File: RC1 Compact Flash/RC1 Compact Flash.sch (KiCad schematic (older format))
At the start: 16 parts, among them J1 Expansion, J2 ADDRESS, J3 ADAPTER, J4 POWER, J5 POWER, U1 74LS00, U3 74LS138, U4 74LS138

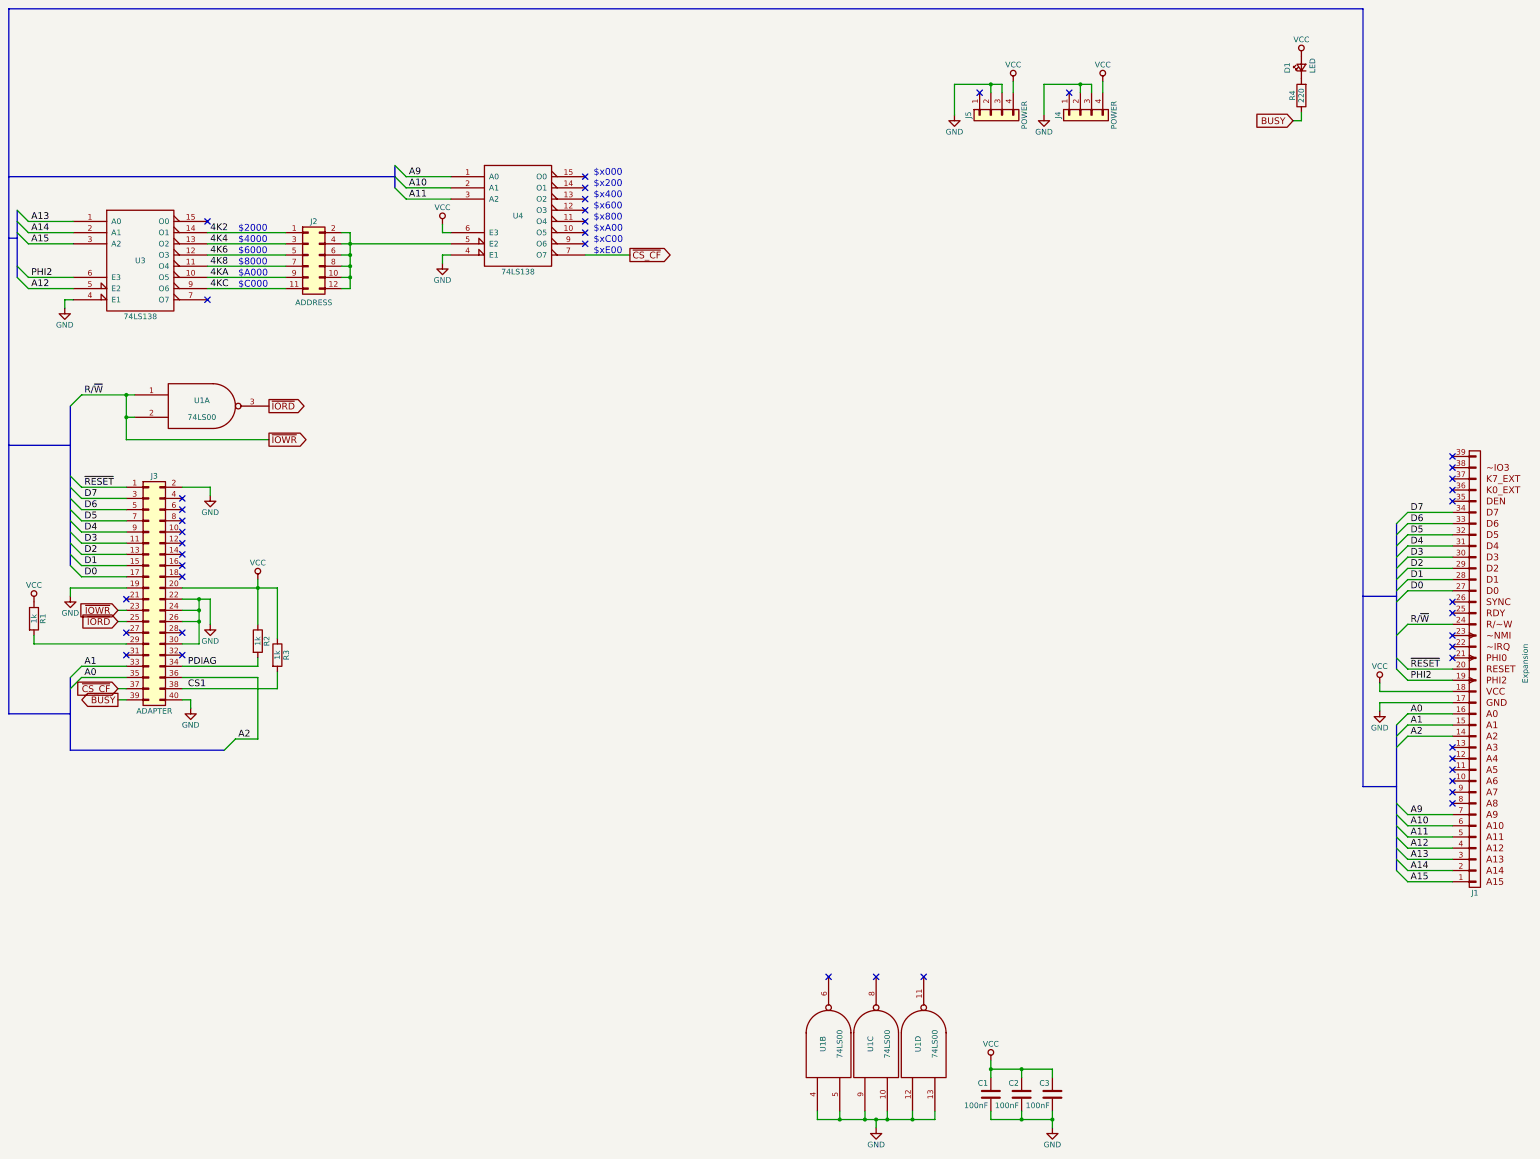
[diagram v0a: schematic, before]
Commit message: Added buffer to Compact Flash
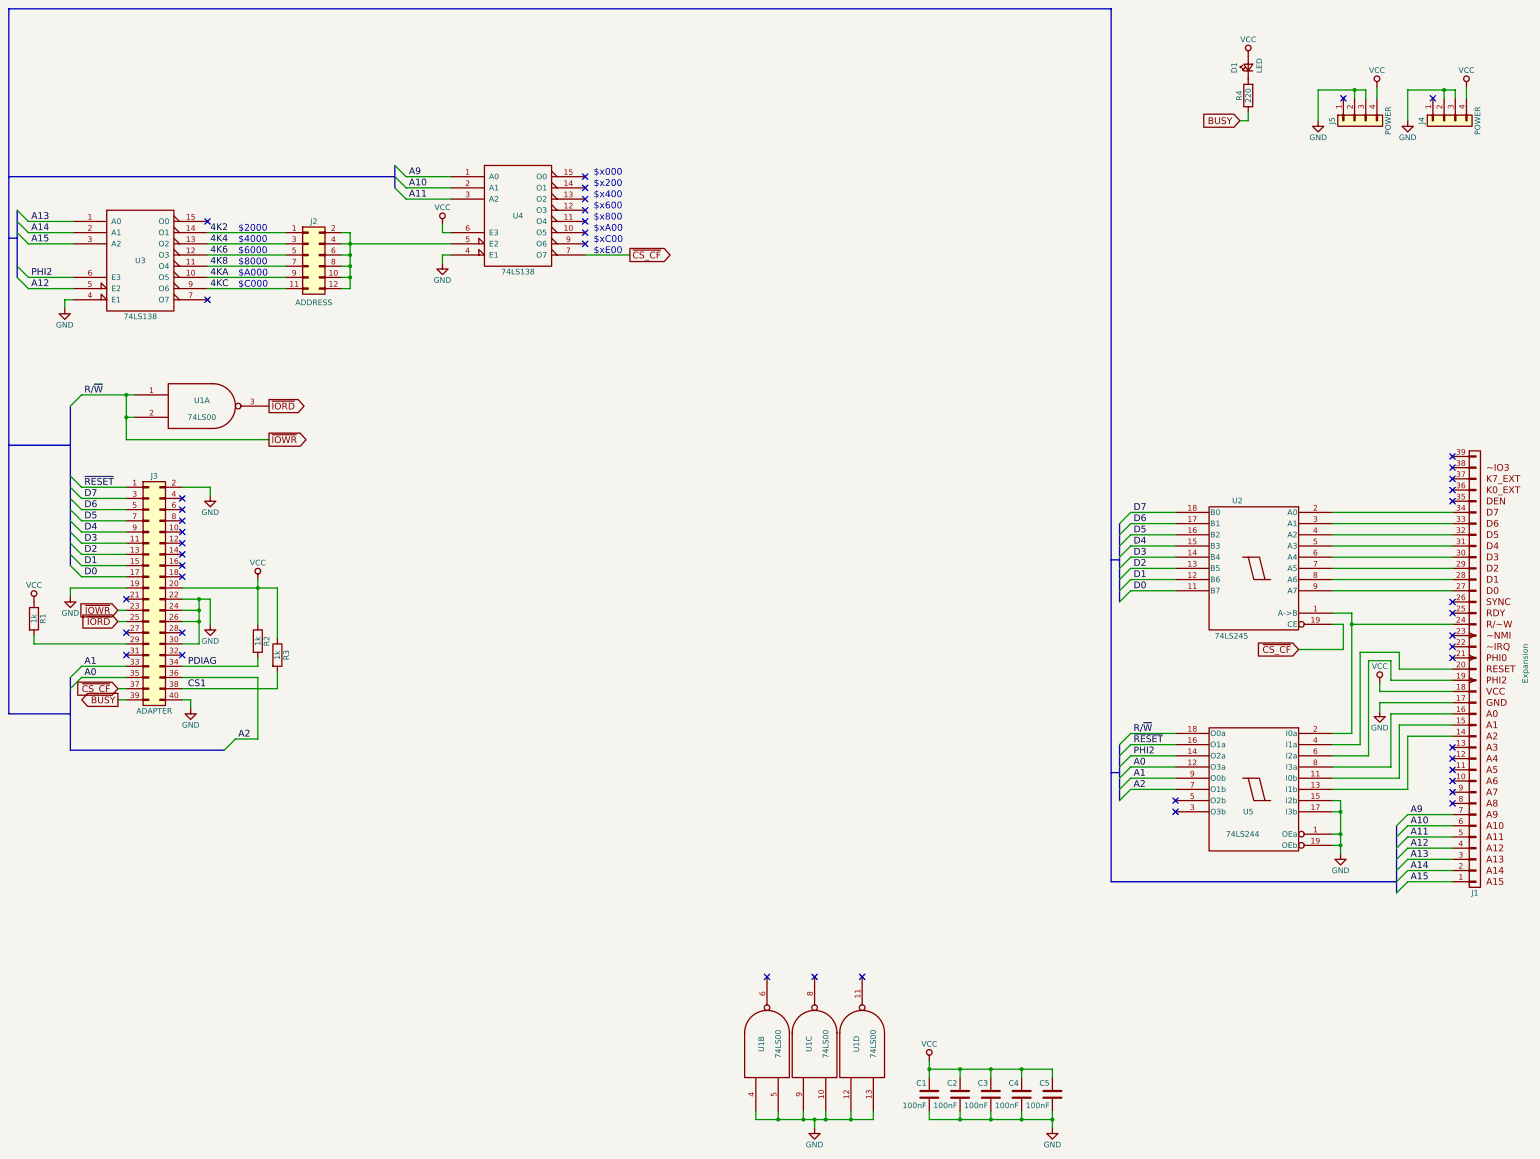
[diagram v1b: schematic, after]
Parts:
- added C4, C5: 100nF, Capacitors_THT:C_Disc_D4.7mm_W2.5mm_P5.00mm, symbol C
- added U2: 74LS245, Housings_DIP:DIP-20_W7.62mm_Socket_LongPads, symbol 74LS245
- added U5: 74LS244, Housings_DIP:DIP-20_W7.62mm_Socket_LongPads, symbol 74LS244
- U3, U4: footprint Housings_DIP:DIP-16_W7.62mm_Socket -> Housings_DIP:DIP-16_W7.62mm_Socket_LongPads
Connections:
- net A0: now also U5.12 (O3a); no longer J1.16 (A0)
- net A1: now also U5.9 (O0b); no longer J1.15 (A1)
- net A2: now also U5.7 (O1b); no longer J1.14 (A2)
- net D0: now also U2.11 (B7); no longer J1.27 (D0)
- net D1: now also U2.12 (B6); no longer J1.28 (D1)
- net D2: now also U2.13 (B5); no longer J1.29 (D2)
- net D3: now also U2.14 (B4); no longer J1.30 (D3)
- net D4: now also U2.15 (B3); no longer J1.31 (D4)
- net D5: now also U2.16 (B2); no longer J1.32 (D5)
- net D6: now also U2.17 (B1); no longer J1.33 (D6)
- net D7: now also U2.18 (B0); no longer J1.34 (D7)
- net GND: now also C4.2, C5.2, U2.10 (GND), U5.1 (OEa), U5.10 (GND), U5.15 (I2b), U5.17 (I3b), U5.19 (OEb)
- net PHI2: now also U5.14 (O2a); no longer J1.19 (PHI2)
- net VCC: now also C4.1, C5.1, U2.20 (VCC), U5.20 (VCC)
- net ~CS_CF: now also U2.19 (CE)
- net ~IOWR: now also U5.18 (O0a); no longer J1.24 (RW)
- net ~RESET: now also U5.16 (O1a); no longer J1.20 (RESET)
- new net: J1.14 (A2), U5.13 (I1b)
- new net: J1.15 (A1), U5.11 (I0b)
- new net: J1.16 (A0), U5.8 (I3a)
- new net: J1.19 (PHI2), U5.6 (I2a)
- new net: J1.20 (RESET), U5.4 (I1a)
- new net: J1.24 (RW), U2.1 (A->B), U5.2 (I0a)
- new net: J1.27 (D0), U2.9 (A7)
- new net: J1.28 (D1), U2.8 (A6)
- new net: J1.29 (D2), U2.7 (A5)
- new net: J1.30 (D3), U2.6 (A4)
- new net: J1.31 (D4), U2.5 (A3)
- new net: J1.32 (D5), U2.4 (A2)
- new net: J1.33 (D6), U2.3 (A1)
- new net: J1.34 (D7), U2.2 (A0)
- no-connect marks 43 -> 45
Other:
- moved on the sheet: C1, C2, C3, D1, J4, J5, R4, U1B, U1C, U1D
